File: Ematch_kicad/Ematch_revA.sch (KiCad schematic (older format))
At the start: 39 parts, among them J1 Conn_01x02_Female, U3 INA138

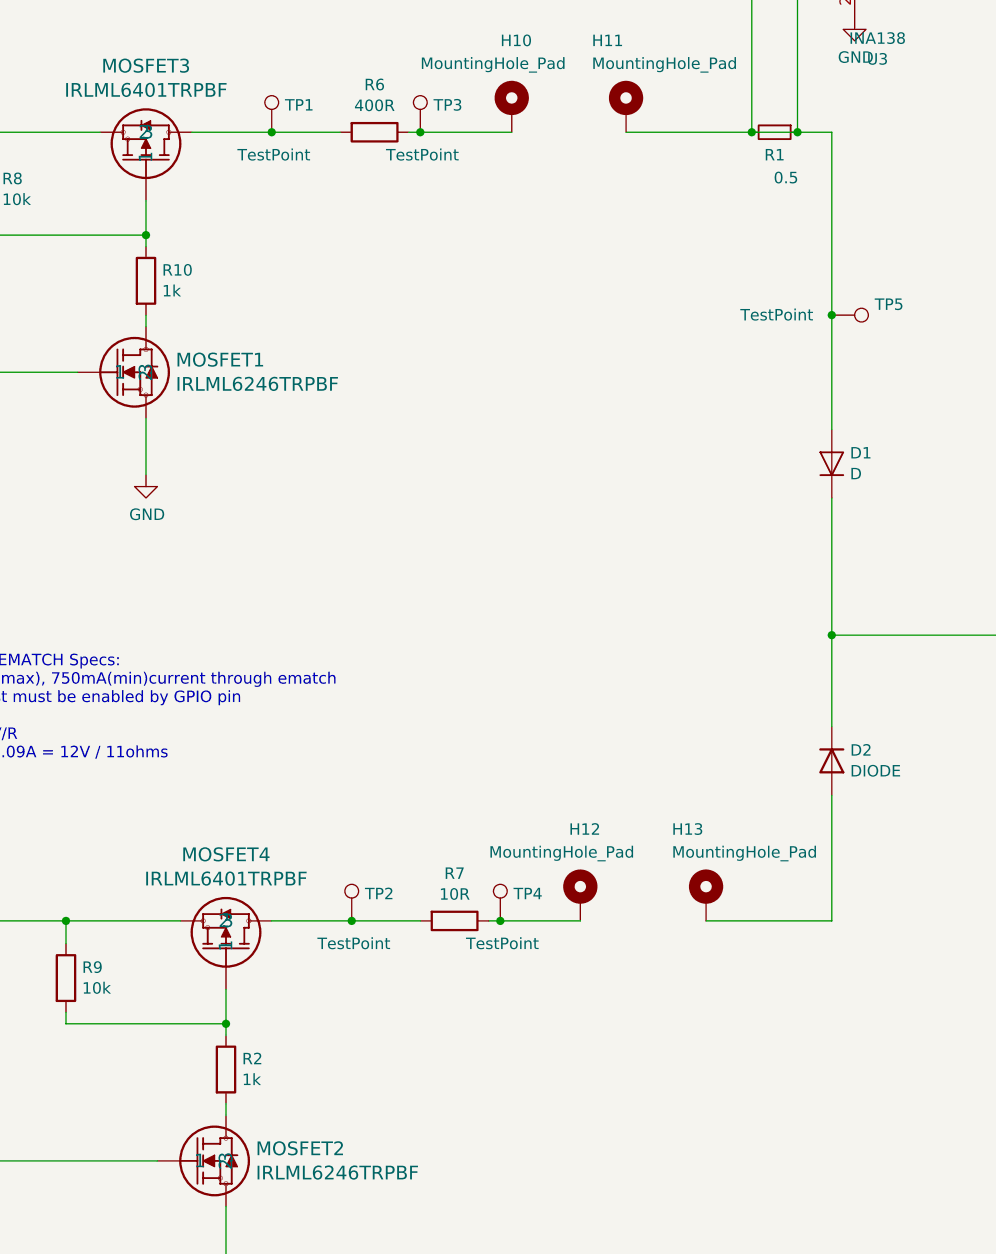
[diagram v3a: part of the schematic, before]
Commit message: added amatch requirements text
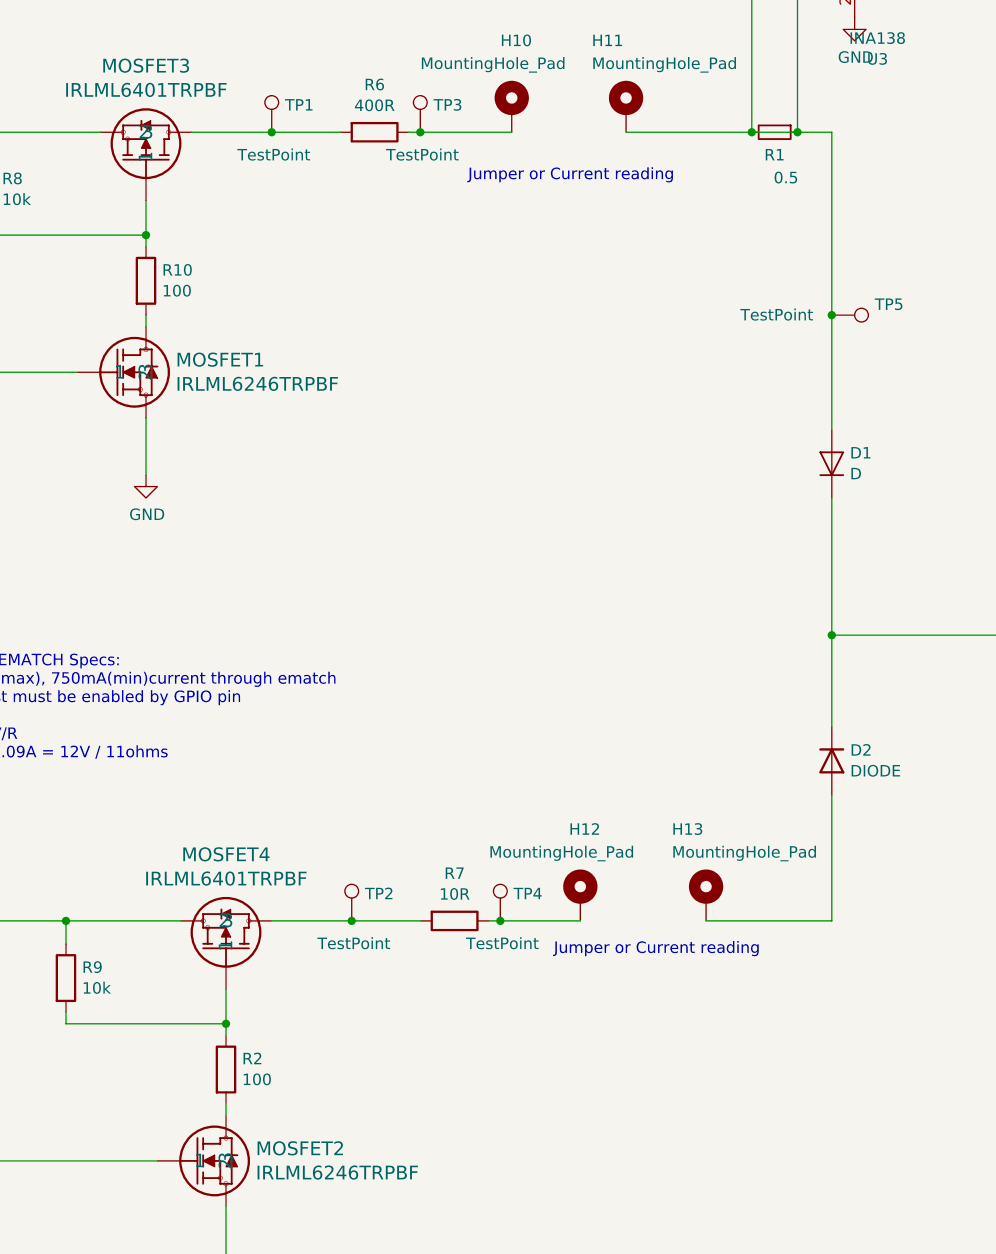
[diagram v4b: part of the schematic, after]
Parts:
- R10, R2: value 1k -> 100
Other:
- note added: "Jumper or Current reading"
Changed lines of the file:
@@
 P 5600 5850
 F 0 "R2" H 5670 5896 50  0000 L CNN
-F 1 "1k" H 5670 5805 50  0000 L CNN
+F 1 "100" H 5670 5805 50  0000 L CNN
 F 2 "Resistor_SMD:R_0805_2012Metric_Pad1.15x1.40mm_HandSolder" V 5530 5850 50  0001 C CNN
 F 3 "~" H 5600 5850 50  0001 C CNN
@@
 P 5250 2400
 F 0 "R10" H 5320 2446 50  0000 L CNN
-F 1 "1k" H 5320 2355 50  0000 L CNN
+F 1 "100" H 5320 2355 50  0000 L CNN
 F 2 "Resistor_SMD:R_0805_2012Metric_Pad1.15x1.40mm_HandSolder" V 5180 2400 50  0001 C CNN
 F 3 "~" H 5250 2400 50  0001 C CNN
@@
 $EndComp
 $Comp
+L Device:R R11
+U 1 1 60FD2586
+P 9800 4400
+F 0 "R11" H 9870 4446 50  0000 L CNN
+F 1 "R" H 9870 4355 50  0000 L CNN
+F 2 "Resistor_THT:R_Axial_DIN0411_L9.9mm_D3.6mm_P15.24mm_Horizontal" V 9730 4400 50  0001 C CNN
+F 3 "~" H 9800 4400 50  0001 C CNN
+	1    9800 4400
+	1    0    0    -1
+$EndComp
+Connection ~ 9800 4100
+Wire Wire Line
+	9800 4100 9800 3950
+Connection ~ 9800 4600
+Wire Wire Line
+	9800 4600 9800 4700
+$Comp
+L Mechanical:MountingHole_Pad H11
+U 1 1 60F912D9
+P 7350 1650
+F 0 "H11" H 7200 1950 50  0000 L CNN
+F 1 "MountingHole_Pad" H 7200 1850 50  0000 L CNN
+F 2 "Connector_Pin:Pin_D1.3mm_L11.0mm" H 7350 1650 50  0001 C CNN
+F 3 "~" H 7350 1650 50  0001 C CNN
+	1    7350 1650
+	1    0    0    -1
+$EndComp
+$Comp
+L Connector:TestPoint TP3
+U 1 1 60F73E80
+P 6450 1750
+F 0 "TP3" H 6508 1868 50  0000 L CNN
+F 1 "TestPoint" H 6300 1650 50  0000 L CNN
+F 2 "TestPoint:TestPoint_Pad_D1.5mm" H 6650 1750 50  0001 C CNN
+F 3 "~" H 6650 1750 50  0001 C CNN
+	1    6450 1750
+	1    0    0    -1
+$EndComp
+Connection ~ 6450 1750
+Wire Wire Line
+	7350 1750 7900 1750
+Wire Wire Line
+	6450 1750 6850 1750
+Connection ~ 6800 5200
+Wire Wire Line
+	7700 5200 8250 5200
+Wire Wire Line
+	6800 5200 7150 5200
+$Comp
+L Connector:Conn_01x02_Female J1
+U 1 1 610021F8
+P 1550 6900
+F 0 "J1" H 1578 6876 50  0000 L CNN
+F 1 "Conn_01x02_Female" H 1578 6785 50  0000 L CNN
+F 2 "Connector_USB:USB_C_Plug_Molex_105444" H 1550 6900 50  0001 C CNN
+F 3 "~" H 1550 6900 50  0001 C CNN
+	1    1550 6900
+	1    0    0    -1
+$EndComp
+Wire Wire Line
+	1350 7000 1350 7100
+$Comp
+L power:GND #PWR012
+U 1 1 61003D5B
+P 1350 7100
+F 0 "#PWR012" H 1350 6850 50  0001 C CNN
+F 1 "GND" H 1355 6927 50  0000 C CNN
+F 2 "" H 1350 7100 50  0001 C CNN
+F 3 "" H 1350 7100 50  0001 C CNN
+	1    1350 7100
+	1    0    0    -1
+$EndComp
+Wire Wire Line
+	1350 6900 1350 6650
+$Comp
+L power:+12V #PWR011
+U 1 1 61005C28
+P 1350 6650
+F 0 "#PWR011" H 1350 6500 50  0001 C CNN
+F 1 "+12V" H 1365 6823 50  0000 C CNN
+F 2 "" H 1350 6650 50  0001 C CNN
+F 3 "" H 1350 6650 50  0001 C CNN
+	1    1350 6650
+	1    0    0    -1
+$EndComp
+$Comp
+L Mechanical:MountingHole_Pad H14
+U 1 1 61023456
+P 1350 4200
+F 0 "H14" V 1400 4450 50  0000 L CNN
+F 1 "MountingHole_Pad" V 1300 4450 50  0000 L CNN
+F 2 "Connector_Pin:Pin_D1.0mm_L10.0mm" H 1350 4200 50  0001 C CNN
+F 3 "~" H 1350 4200 50  0001 C CNN
+	1    1350 4200
+	0    1    1    0
+$EndComp
+$Comp
+L power:GND #PWR013
+U 1 1 61025BD0
+P 1250 4400
+F 0 "#PWR013" H 1250 4150 50  0001 C CNN
+F 1 "GND" H 1255 4227 50  0000 C CNN
+F 2 "" H 1250 4400 50  0001 C CNN
+F 3 "" H 1250 4400 50  0001 C CNN
+	1    1250 4400
+	1    0    0    -1
+$EndComp
+Wire Wire Line
+	1250 4400 1250 4200
+$Comp
 L Device:R R7
 U 1 1 60F9B8E0
@@
 	0    1    1    0
 $EndComp
-$Comp
-L Device:R R11
-U 1 1 60FD2586
-P 9800 4400
-F 0 "R11" H 9870 4446 50  0000 L CNN
-F 1 "R" H 9870 4355 50  0000 L CNN
-F 2 "Resistor_THT:R_Axial_DIN0411_L9.9mm_D3.6mm_P15.24mm_Horizontal" V 9730 4400 50  0001 C CNN
-F 3 "~" H 9800 4400 50  0001 C CNN
-	1    9800 4400
-	1    0    0    -1
-$EndComp
-Connection ~ 9800 4100
-Wire Wire Line
-	9800 4100 9800 3950
-Connection ~ 9800 4600
-Wire Wire Line
-	9800 4600 9800 4700
-$Comp
-L Mechanical:MountingHole_Pad H11
-U 1 1 60F912D9
-P 7350 1650
-F 0 "H11" H 7200 1950 50  0000 L CNN
-F 1 "MountingHole_Pad" H 7200 1850 50  0000 L CNN
-F 2 "Connector_Pin:Pin_D1.3mm_L11.0mm" H 7350 1650 50  0001 C CNN
-F 3 "~" H 7350 1650 50  0001 C CNN
-	1    7350 1650
-	1    0    0    -1
-$EndComp
-$Comp
-L Connector:TestPoint TP3
-U 1 1 60F73E80
-P 6450 1750
-F 0 "TP3" H 6508 1868 50  0000 L CNN
-F 1 "TestPoint" H 6300 1650 50  0000 L CNN
-F 2 "TestPoint:TestPoint_Pad_D1.5mm" H 6650 1750 50  0001 C CNN
-F 3 "~" H 6650 1750 50  0001 C CNN
-	1    6450 1750
-	1    0    0    -1
-$EndComp
-Connection ~ 6450 1750
-Wire Wire Line
-	7350 1750 7900 1750
-Wire Wire Line
-	6450 1750 6850 1750
-Connection ~ 6800 5200
-Wire Wire Line
-	7700 5200 8250 5200
-Wire Wire Line
-	6800 5200 7150 5200
-$Comp
-L Connector:Conn_01x02_Female J1
-U 1 1 610021F8
-P 1550 6900
-F 0 "J1" H 1578 6876 50  0000 L CNN
-F 1 "Conn_01x02_Female" H 1578 6785 50  0000 L CNN
-F 2 "Connector_USB:USB_C_Plug_Molex_105444" H 1550 6900 50  0001 C CNN
-F 3 "~" H 1550 6900 50  0001 C CNN
-	1    1550 6900
-	1    0    0    -1
-$EndComp
-Wire Wire Line
-	1350 7000 1350 7100
-$Comp
-L power:GND #PWR012
-U 1 1 61003D5B
-P 1350 7100
-F 0 "#PWR012" H 1350 6850 50  0001 C CNN
-F 1 "GND" H 1355 6927 50  0000 C CNN
-F 2 "" H 1350 7100 50  0001 C CNN
-F 3 "" H 1350 7100 50  0001 C CNN
-	1    1350 7100
-	1    0    0    -1
-$EndComp
-Wire Wire Line
-	1350 6900 1350 6650
-$Comp
-L power:+12V #PWR011
-U 1 1 61005C28
-P 1350 6650
-F 0 "#PWR011" H 1350 6500 50  0001 C CNN
-F 1 "+12V" H 1365 6823 50  0000 C CNN
-F 2 "" H 1350 6650 50  0001 C CNN
-F 3 "" H 1350 6650 50  0001 C CNN
-	1    1350 6650
-	1    0    0    -1
-$EndComp
-$Comp
-L Mechanical:MountingHole_Pad H14
-U 1 1 61023456
-P 1350 4200
-F 0 "H14" V 1400 4450 50  0000 L CNN
-F 1 "MountingHole_Pad" V 1300 4450 50  0000 L CNN
-F 2 "Connector_Pin:Pin_D1.0mm_L10.0mm" H 1350 4200 50  0001 C CNN
-F 3 "~" H 1350 4200 50  0001 C CNN
-	1    1350 4200
-	0    1    1    0
-$EndComp
-$Comp
-L power:GND #PWR013
-U 1 1 61025BD0
-P 1250 4400
-F 0 "#PWR013" H 1250 4150 50  0001 C CNN
-F 1 "GND" H 1255 4227 50  0000 C CNN
-F 2 "" H 1250 4400 50  0001 C CNN
-F 3 "" H 1250 4400 50  0001 C CNN
-	1    1250 4400
-	1    0    0    -1
-$EndComp
-Wire Wire Line
-	1250 4400 1250 4200
+Text Notes 6659 1971 0    50   ~ 0
+Jumper or Current reading
+Text Notes 7034 5356 0    50   ~ 0
+Jumper or Current reading
 $EndSCHEMATC
